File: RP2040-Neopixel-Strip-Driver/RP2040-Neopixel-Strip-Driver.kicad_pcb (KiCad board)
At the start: 4 copper layers, 10.2 x 47 mm, 43 parts, among them J201 TYPE-C-31-M-12, J202 Conn_01x03, J203 NeopixelStrip, SW202 ~{USB_BOOT}, U201 XC6206P332MR, U202 RP2040, U205 W25Q128JVPIQ, Y201 Crystal_GND24

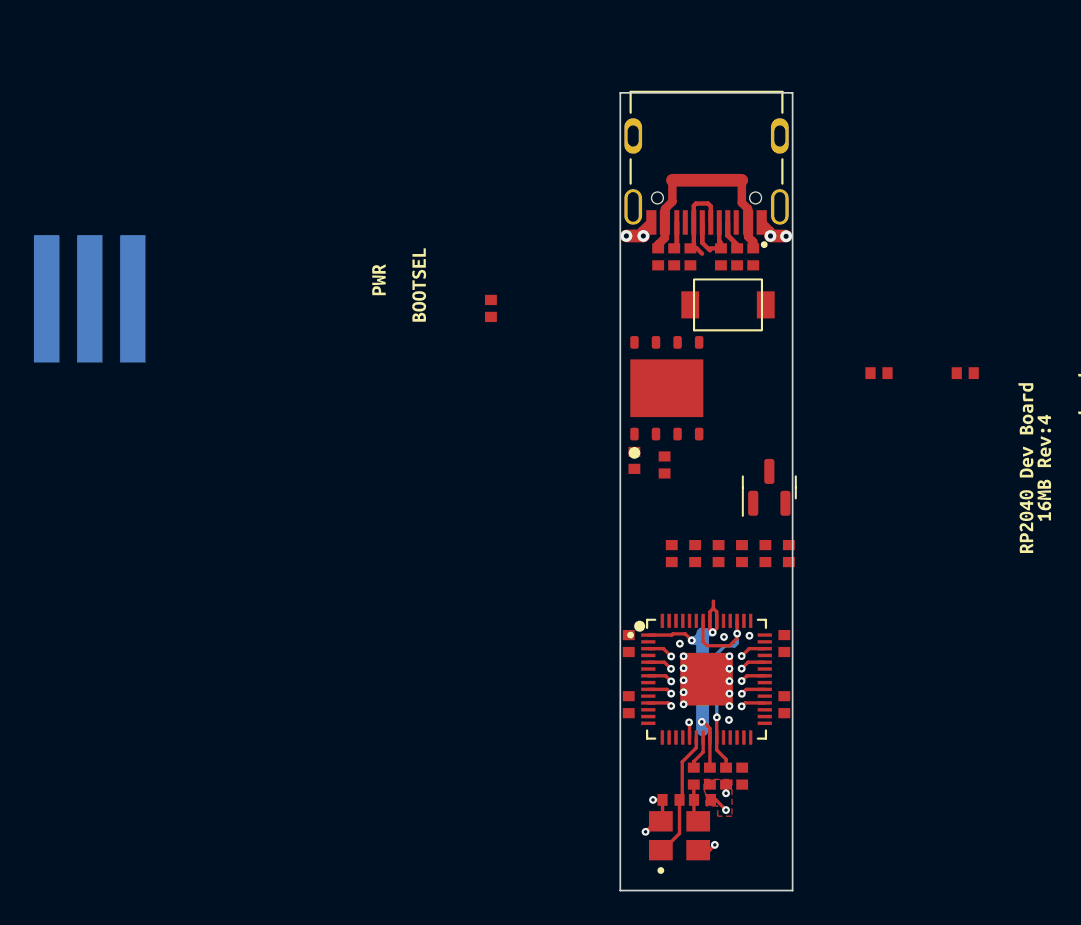
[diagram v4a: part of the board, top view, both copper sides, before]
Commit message: Continued to shrink board.
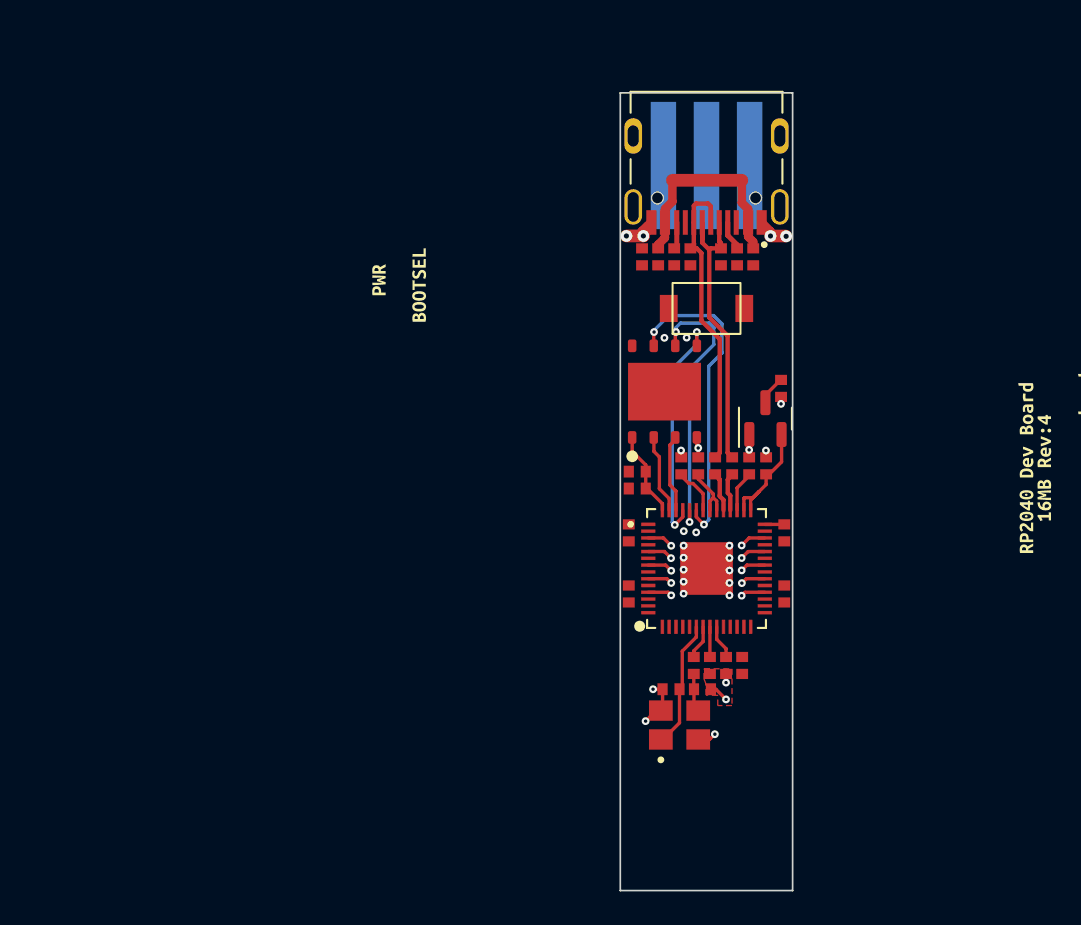
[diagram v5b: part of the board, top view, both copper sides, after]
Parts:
- removed C207: 10uF, Breadstick Footprints:Perfect_0402_Cap
- moved J203 37.2 mm to (146.9, 31.0)
- moved C201 10.9 mm to (151.3, 44.2), turned to 180 degrees
- moved C222 9.40 mm to (143.1, 36.4)
- moved C202 6.52 mm to (148.1, 60.5)
- moved C212 6.52 mm to (142.3, 52.7)
- moved C216 6.52 mm to (151.5, 52.7)
- moved C218 6.52 mm to (147.1, 60.5)
- moved C221 6.52 mm to (149.0, 60.5)
- moved R201 6.52 mm to (146.2, 60.5)
- moved C203 6.52 mm to (144.8, 61.9)
- moved C206 6.52 mm to (146.7, 61.9)
- moved C213 6.52 mm to (151.5, 56.3)
- moved C215 6.52 mm to (142.3, 56.3)
- moved U202 6.52 mm to (146.9, 54.8)
- moved Y201 6.52 mm to (145.3, 64.0)
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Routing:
- net /RP2040/MCU_QSPI_SD3: track 0.00 -> 18.8 mm, vias 0 -> 2
- net /RP2040/MCU_QSPI_SCLK: track 0.00 -> 16.3 mm, vias 0 -> 2
- net /RP2040/USB_D-: track 5.05 -> 19.1 mm
- net /RP2040/MCU_QSPI_SD0: track 0.00 -> 13.9 mm, vias 0 -> 2
- net /RP2040/USB_D+: track 5.49 -> 18.0 mm
- net +1V1: track 13.5 -> 7.20 mm, vias 2 -> 0
- net /RP2040/MCU_QSPI_CSN: track 0.00 -> 5.08 mm
- net /RP2040/MCU_QSPI_SD1: track 0.00 -> 4.66 mm
- net /RP2040/MCU_QSPI_SD2: track 0.00 -> 4.57 mm
- net GND: track 11.4 -> 14.3 mm, vias 24 -> 28
- net 3V3_LDO: track 16.4 -> 13.5 mm, vias 3 -> 0
- net /RP2040/MCU_USB_D+: track 0.00 -> 2.32 mm
- net /RP2040/MCU_USB_D-: track 0.00 -> 2.28 mm
- net VHI: track 0.00 -> 1.74 mm

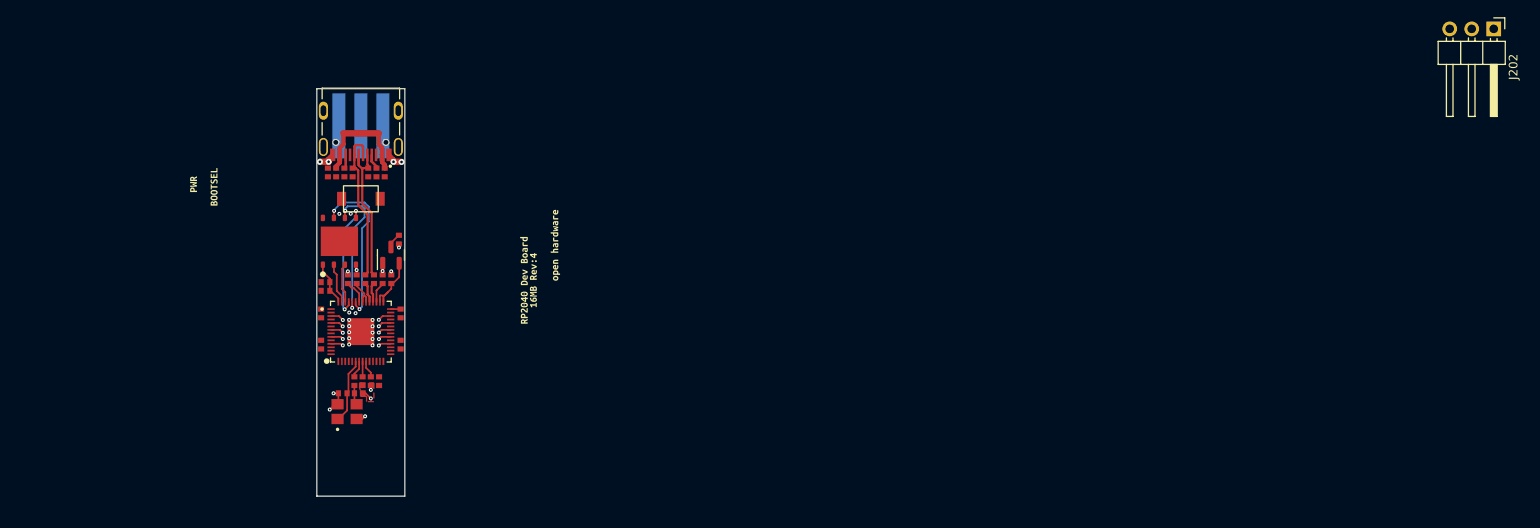
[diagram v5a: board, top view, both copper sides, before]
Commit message: Added bulk decoupling capacitors and PTC resetable fuse, planning level shifter.
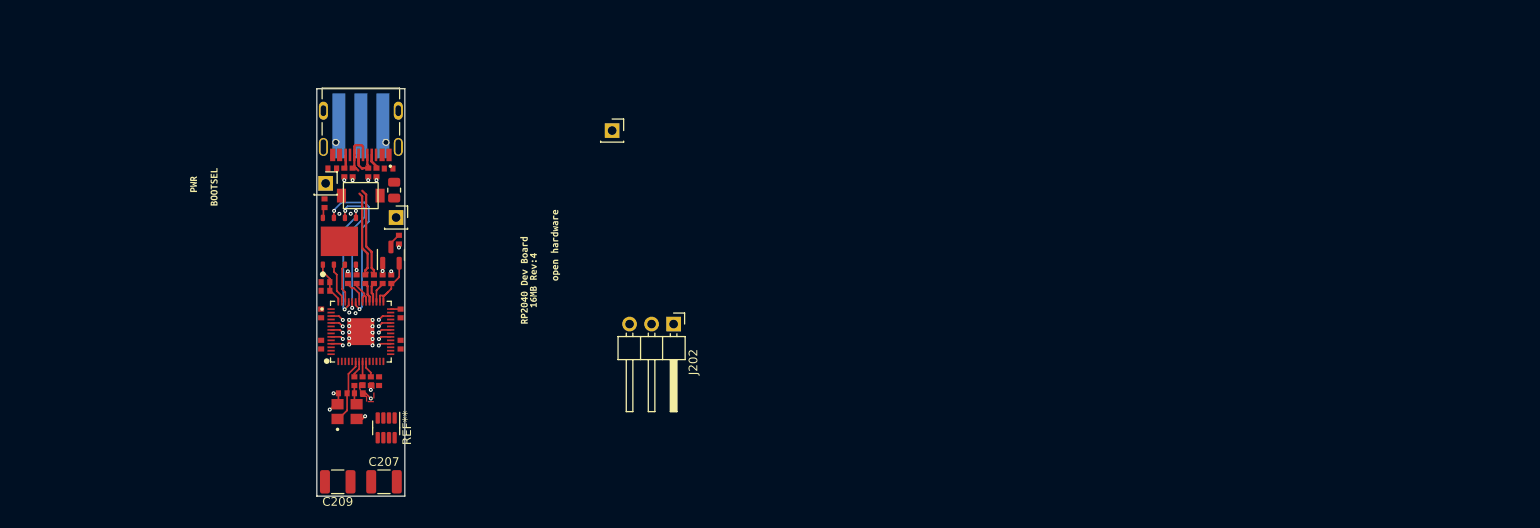
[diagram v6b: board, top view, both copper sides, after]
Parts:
- added C207: 220uF, Capacitor_SMD:C_1210_3225Metric, F.Cu at (149.6, 72.1)
- added C209: 220uF, Capacitor_SMD:C_1210_3225Metric, F.Cu at (144.2, 72.1)
- added F201: 1.5A, 3A Trip, Resistor_SMD:R_0805_2012Metric, F.Cu at (150.8, 38.5)
- added J204: 5V, Connector_PinSocket_2.54mm:PinSocket_1x01_P2.54mm_Vertical, F.Cu at (151.0, 41.6)
- added J205: TO BE DECIDED, Connector_PinSocket_2.54mm:PinSocket_1x01_P2.54mm_Vertical, F.Cu at (175.9, 31.6)
- added J206: GND, Connector_PinSocket_2.54mm:PinSocket_1x01_P2.54mm_Vertical, F.Cu at (142.8, 37.7)
- added REF**: SOT-23-8, Package_TO_SOT_SMD:SOT-23-8, F.Cu at (149.8, 65.9)
- moved J202 100.5 mm to (183.0, 53.9)
- moved C222 3.57 mm to (142.7, 40.0)
- moved D205 0.64 mm to (143.6, 36.0), turned to -90 degrees
- moved D203 0.64 mm to (150.1, 36.0), turned to 90 degrees
- moved SW202 0.37 mm to (146.9, 39.1)
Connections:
- C201 pad 1: VHI -> VBUS
- D203 pad 2: VBUS -> Net-(D205-Pad2)
- D205 pad 2: VBUS -> Net-(D205-Pad2)
- J201 pad A4B9: VBUS -> Net-(D205-Pad2)
- J201 pad B4A9: VBUS -> Net-(D205-Pad2)
- U201 pad 3: VHI -> VBUS
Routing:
- net VBUS: track 12.8 -> 1.74 mm
- net /RP2040/USB_D+: track 18.0 -> 15.7 mm
- net GND: track 14.3 -> 12.0 mm
- net /RP2040/USB_D-: track 19.1 -> 16.9 mm
- net VHI: track 1.74 -> 0.00 mm
- net 3V3_LDO: track 13.5 -> 14.8 mm

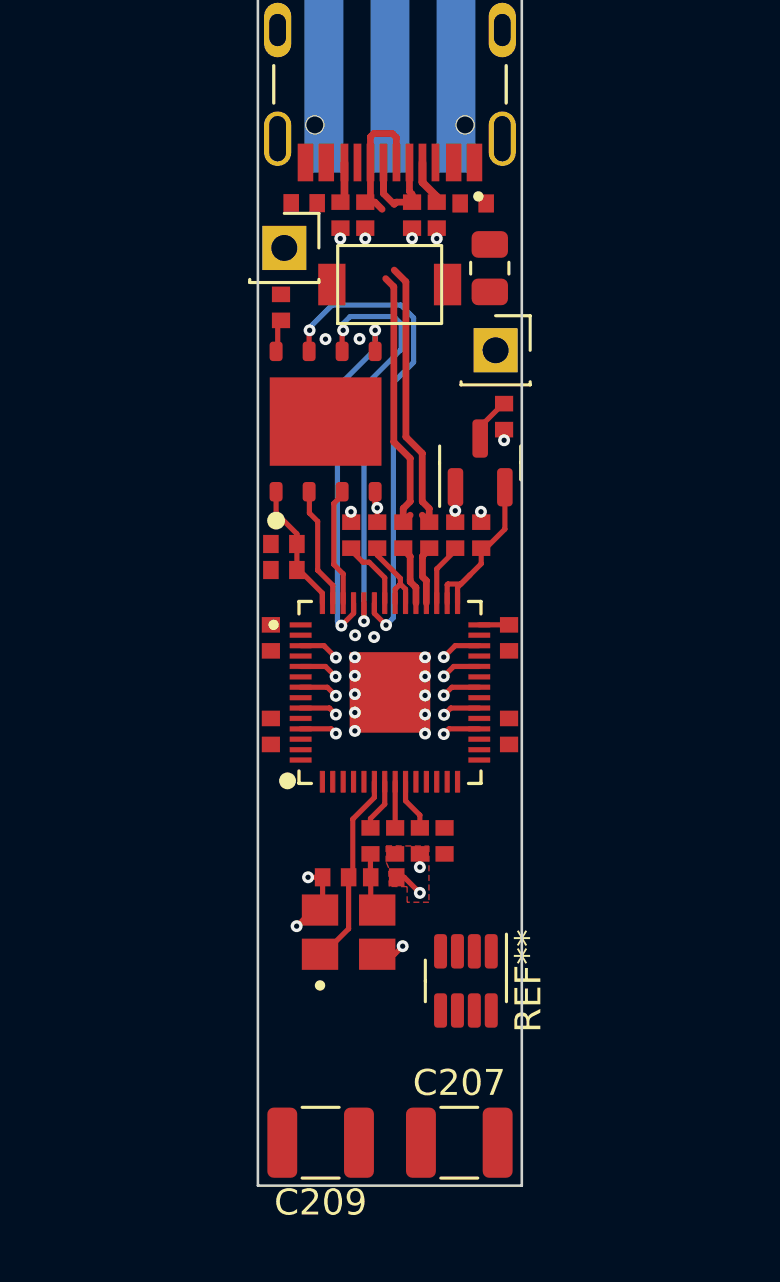
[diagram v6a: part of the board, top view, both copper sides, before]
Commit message: Worked on layout, still selecting a level shifter.
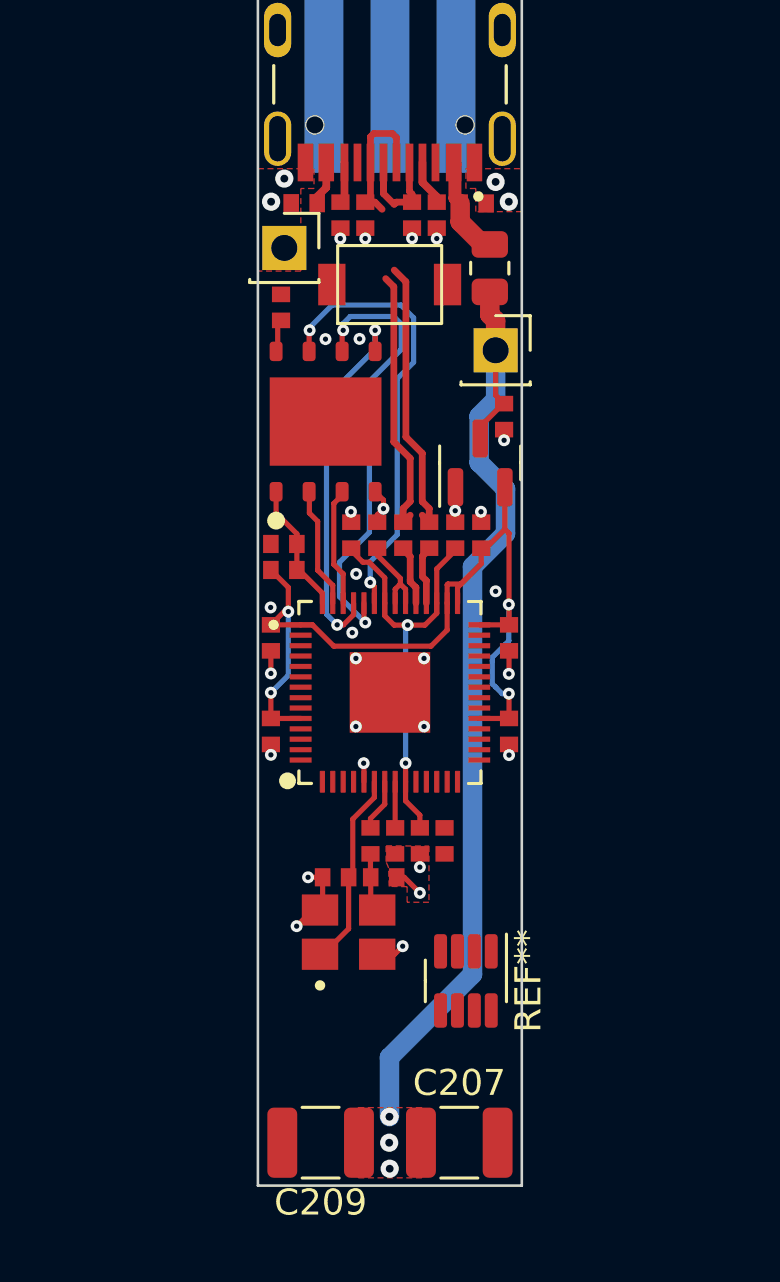
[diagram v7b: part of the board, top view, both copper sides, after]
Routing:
- net VBUS: track 1.74 -> 38.3 mm, vias 0 -> 3
- net 3V3_LDO: track 14.8 -> 41.4 mm, vias 0 -> 4
- net +1V1: track 7.20 -> 16.5 mm, vias 0 -> 2
- net Net-(D205-Pad2): track 0.00 -> 5.60 mm
- net GND: track 12.0 -> 15.4 mm, vias 28 -> 33
- net /RP2040/MCU_QSPI_SD3: track 18.8 -> 17.2 mm
- net GPIO28/ADC2: track 1.55 -> 0.00 mm, vias 1 -> 0
- net GPIO1: track 1.55 -> 0.00 mm, vias 1 -> 0
- net GPIO26/ADC0: track 1.52 -> 0.00 mm, vias 1 -> 0
- net GPIO3: track 1.51 -> 0.00 mm, vias 1 -> 0
- net GPIO24: track 1.49 -> 0.00 mm, vias 1 -> 0
- net GPIO5: track 1.49 -> 0.00 mm, vias 1 -> 0
- net GPIO22: track 1.46 -> 0.00 mm, vias 1 -> 0
- net GPIO7: track 1.46 -> 0.00 mm, vias 1 -> 0
- net GPIO21: track 1.45 -> 0.00 mm, vias 1 -> 0
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- added copper zone on F.Cu, net VBUS

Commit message: Update RP2040-Neopixel-Strip-Driver.kicad_pcb
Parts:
- removed REF**: SOT-23-8, Package_TO_SOT_SMD:SOT-23-8
- moved C209 30.1 mm to (149.6, 42.5)
- moved C207 26.4 mm to (149.6, 45.7), turned to 180 degrees
- moved C202 7.79 mm to (148.1, 68.3)
- moved C204 7.79 mm to (150.4, 56.5)
- moved C205 7.79 mm to (149.4, 56.5)
- moved C208 7.79 mm to (145.4, 56.5)
- moved C218 7.79 mm to (147.1, 68.3)
- moved C219 7.79 mm to (146.4, 56.5)
- moved C221 7.79 mm to (149.0, 68.3)
- moved R201 7.79 mm to (146.2, 68.3)
- moved R203 7.79 mm to (148.4, 56.5)
- moved R204 7.79 mm to (147.4, 56.5)
- moved U205 7.79 mm to (144.4, 52.2)
- moved C201 7.79 mm to (151.3, 52.0)
- moved C203 7.79 mm to (144.8, 69.7)
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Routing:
- net VBUS: track 38.3 -> 14.1 mm, vias 3 -> 0
- net /RP2040/MCU_QSPI_SCLK: track 17.2 -> 1.59 mm
- net /RP2040/MCU_QSPI_SD3: track 17.2 -> 1.68 mm
- net /RP2040/MCU_QSPI_SD0: track 14.3 -> 2.05 mm
- net /RP2040/USB_D+: track 15.7 -> 25.6 mm
- net /RP2040/USB_D-: track 16.9 -> 24.6 mm
- net 3V3_LDO: track 41.4 -> 33.8 mm
- net +1V1: track 16.5 -> 11.1 mm
- net GND: vias 33 -> 37
- net Net-(D205-Pad2): vias 0 -> 1
- removed copper zone on F.Cu, net VBUS
